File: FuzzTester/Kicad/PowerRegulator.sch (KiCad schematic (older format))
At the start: 10 parts, among them J5 TestPower_PinHeader, J6 9V Power JST XH, U1 AMS1117-5.0, U2 AMS1117-3.3

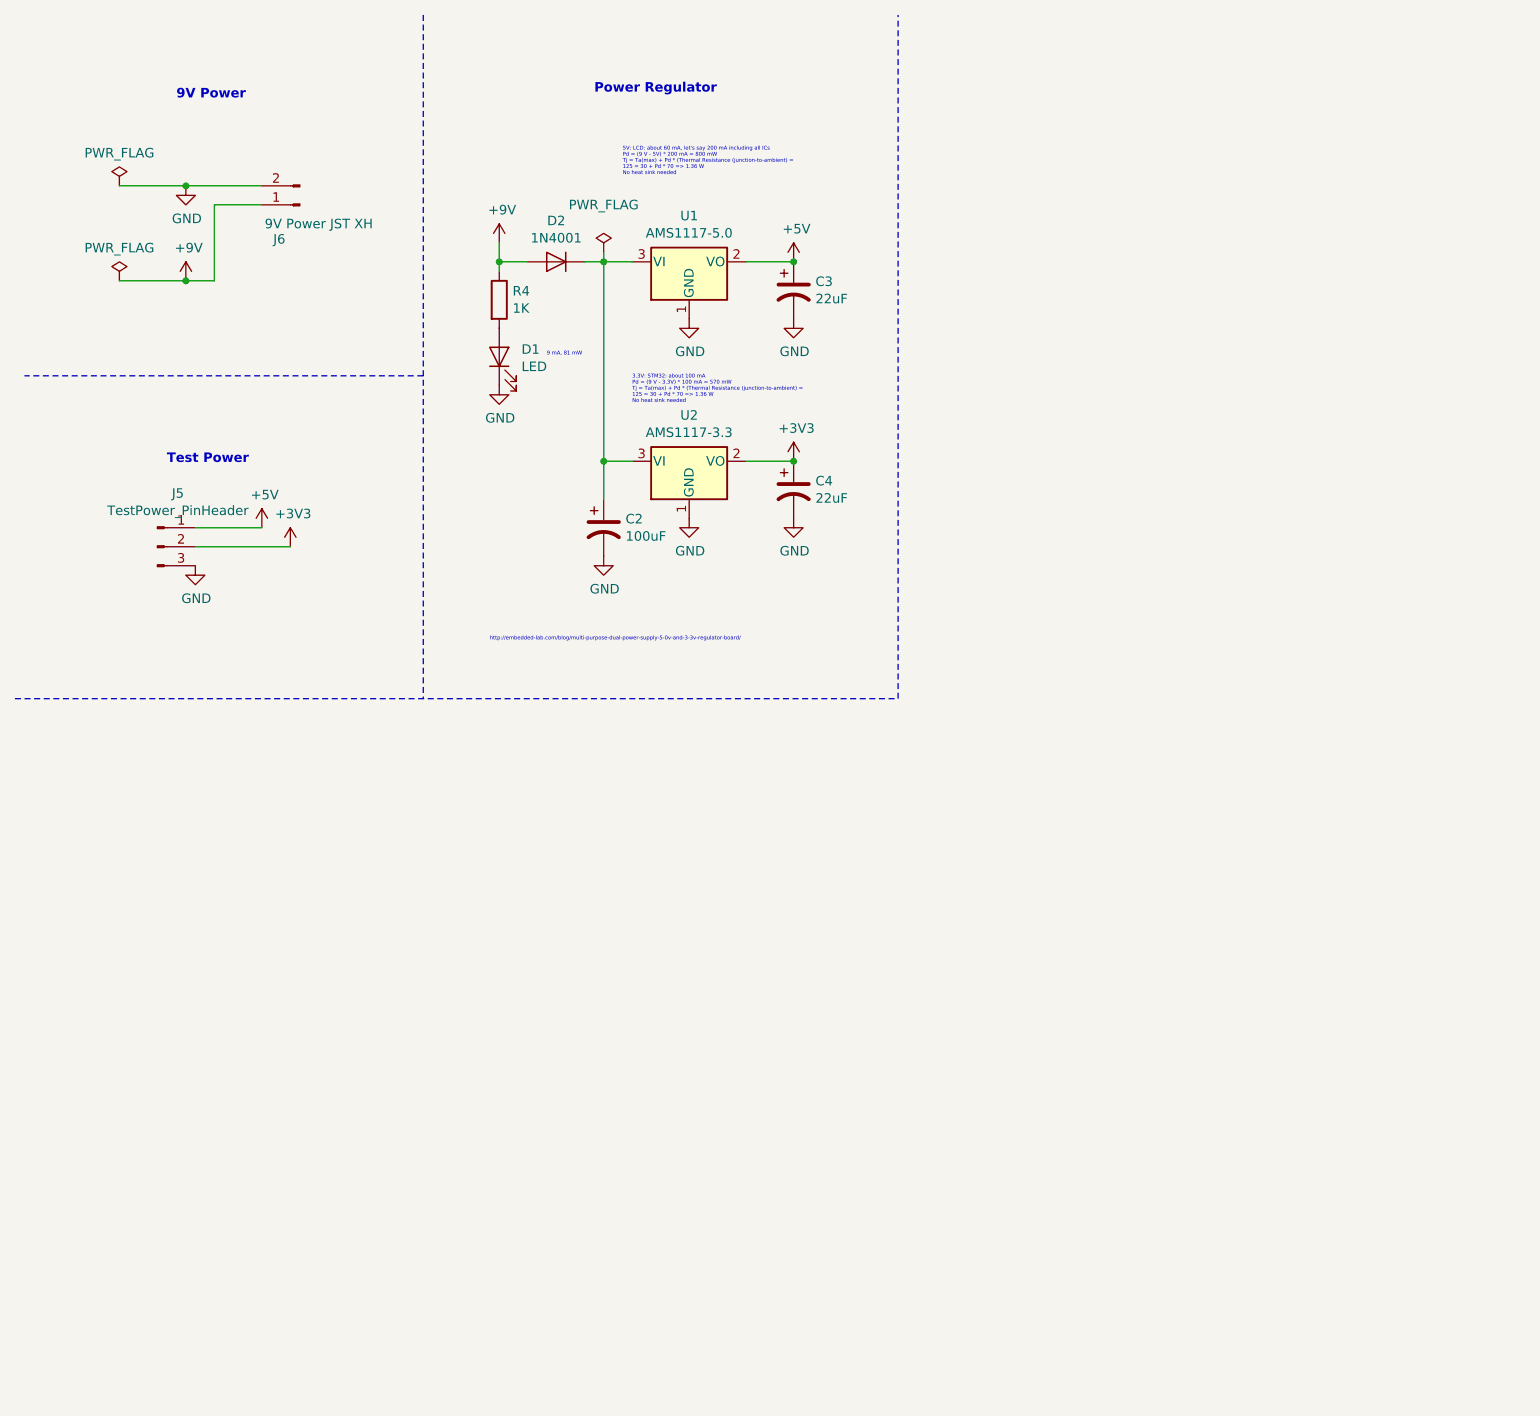
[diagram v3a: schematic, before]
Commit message: Power regulator -9V
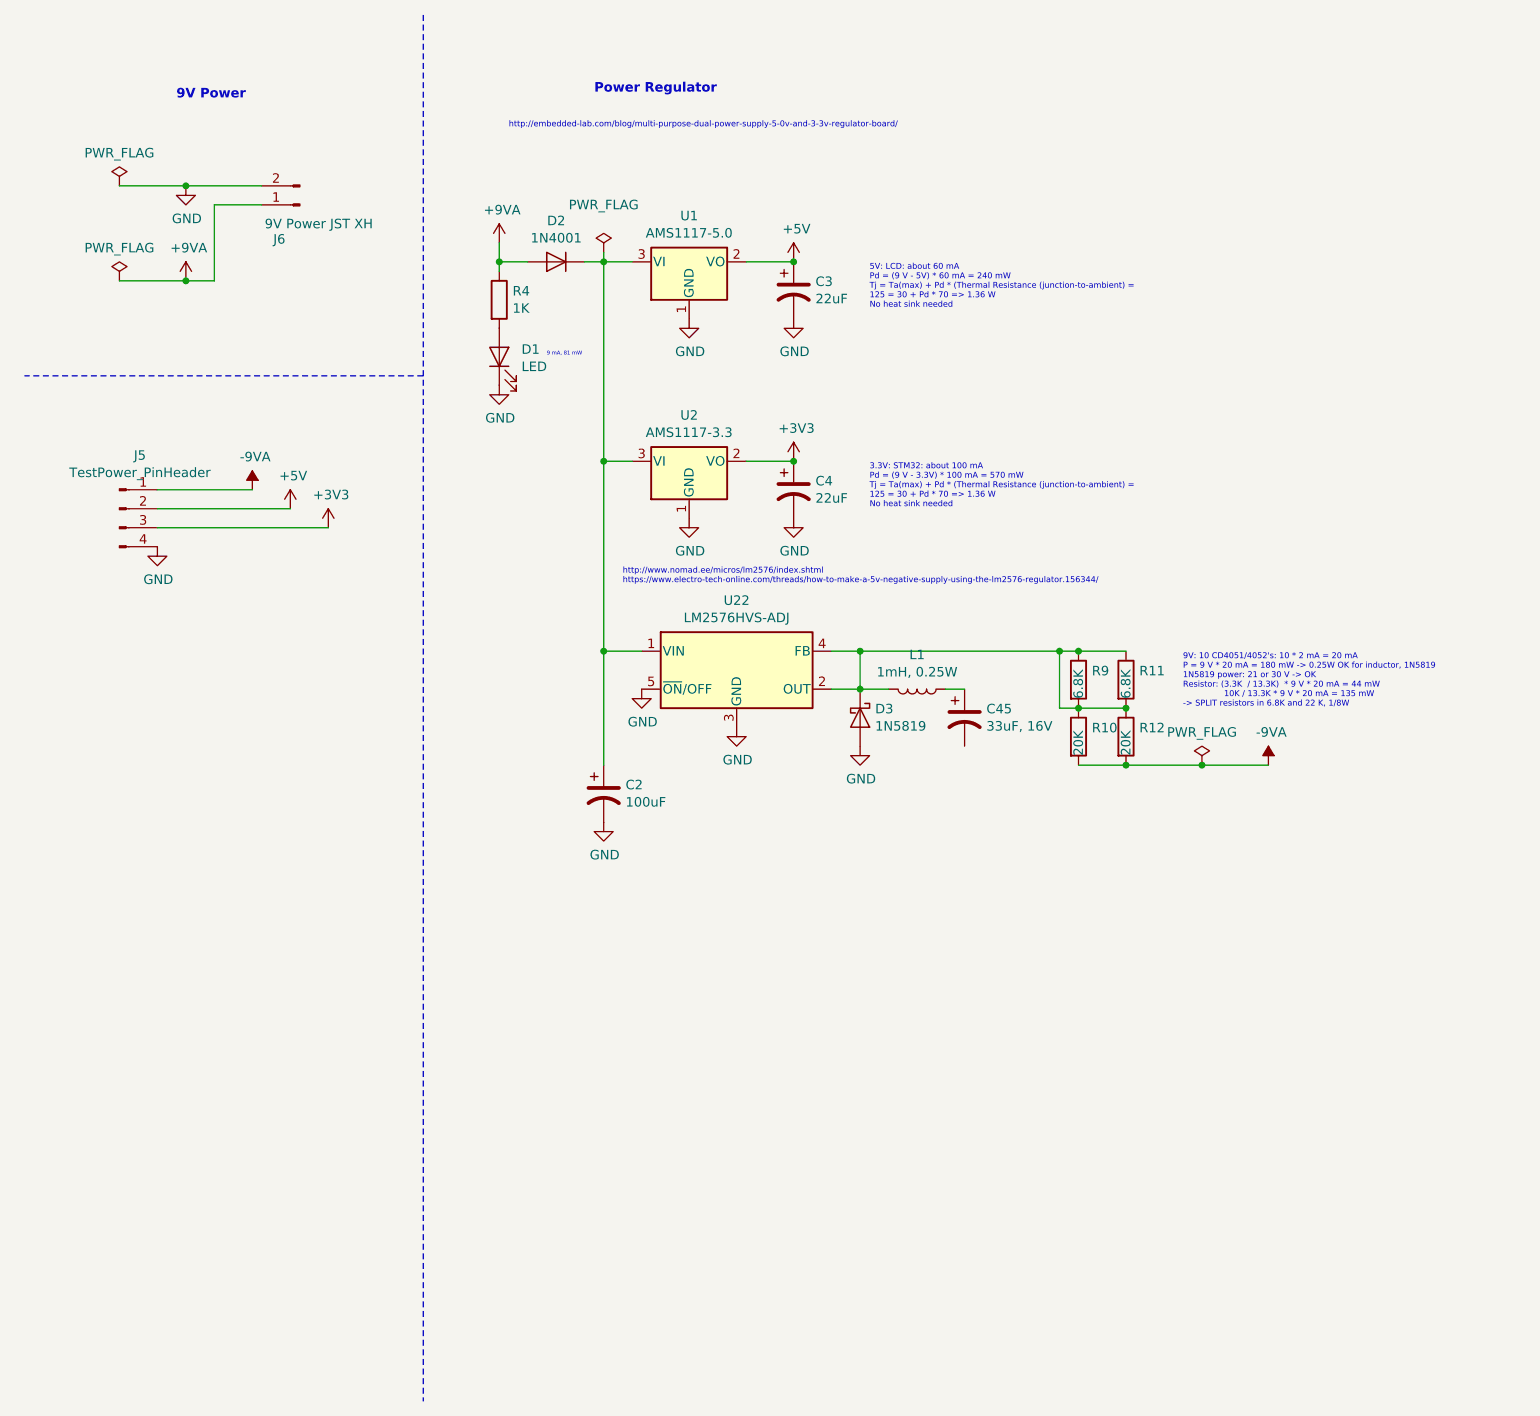
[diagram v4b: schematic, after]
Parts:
- removed J5: TestPower_PinHeader, Connector_PinHeader_2.54mm:PinHeader_1x03_P2.54mm_Vertical, symbol Connector:Conn_01x03_Male
- added C45: 33uF, 16V, symbol Device:CP1
- added D3: 1N5819, Diode_THT:D_DO-41_SOD81_P10.16mm_Horizontal, symbol Diode:1N5819
- added J5: TestPower_PinHeader, symbol Connector:Conn_01x04_Male
- added L1: 1mH, 0.25W, symbol Device:L
- added R10, R12: 20K, symbol Device:R
- added R11, R9: 6.8K, symbol Device:R
- added U22: LM2576HVS-ADJ, Package_TO_SOT_SMD:TO-263-5_TabPin3, symbol Regulator_Switching:LM2576HVS-ADJ
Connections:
- net +3V3: now also J5.3 (Pin_3)
- net +5V: now also J5.2 (Pin_2)
- net GND: now also D3.2 (A), J5.4 (Pin_4), U22.3 (GND), U22.5 (~ON~/OFF)
- net at C2.1, D2.1 (K), U1.3 (VI)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: now also U22.1 (VIN)
- net +9V renamed +9VA
- new net: D3.1 (K), L1.2, R10.1, R11.1, R11.2, R12.1, R9.1, R9.2, U22.2 (OUT), U22.4 (FB)
- new net: C45.1, L1.1
- new net -9VA: J5.1 (Pin_1), R10.2, R12.2
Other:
- note added: "5V: LCD: about 60 mA\nPd = (9 V - 5V) * 60 mA = 240 mW\nTj = Ta(max) + Pd * (Thermal Resistance (junction-to-ambient) =\n125 = 30 + Pd * 70 => 1.36 W\nNo heat sink needed"
- note added: "9V: 10 CD4051/4052's: 10 * 2 mA = 20 mA\nP = 9 V * 20 mA = 180 mW -> 0.25W OK for inductor, 1N5819\n1N5819 power: 21 or 30 V -> OK\nResistor: (3.3K / 13.3K) * 9 V * 20 mA = 44 mW\n 10K / 13.3K * 9 V * 20 mA = 135 mW\n-> SPLIT resistors in 6.8K and 22 K, 1/8W\n"
- note added: "http://www.nomad.ee/micros/lm2576/index.shtml"
- note added: "https://www.electro-tech-online.com/threads/how-to-make-a-5v-negative-supply-using-the-lm2576-regulator.156344/"
- note removed: "5V: LCD: about 60 mA, let's say 200 mA including all ICs\nPd = (9 V - 5V) * 200 mA = 800 mW\nTj = Ta(max) + Pd * (Thermal Resistance (junction-to-ambient) =\n125 = 30 + Pd * 70 => 1.36 W\nNo heat sink needed"
- note removed: "Test Power\n\n"
- moved on the sheet: C2

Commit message: PCB Placement 100x82
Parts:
- removed C45: 33uF, 16V, symbol Device:CP1
- removed D3: 1N5819, Diode_THT:D_DO-41_SOD81_P10.16mm_Horizontal, symbol Diode:1N5819
- removed L1: 1mH, 0.25W, symbol Device:L
- removed R10, R12: 20K, symbol Device:R
- removed R11, R9: 6.8K, symbol Device:R
- removed U22: LM2576HVS-ADJ, Package_TO_SOT_SMD:TO-263-5_TabPin3, symbol Regulator_Switching:LM2576HVS-ADJ
- J5: value TestPower_PinHeader -> PowerTest_PinHeader; footprint (none) -> Connector_PinHeader_2.54mm:PinHeader_1x04_P2.54mm_Vertical
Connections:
- net labels added: +9V
- net labels removed: +9VA, -9VA
- wire segments 36 -> 19
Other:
- note added: "Power Test Connector\n"
- note removed: "9V: 10 CD4051/4052's: 10 * 2 mA = 20 mA\nP = 9 V * 20 mA = 180 mW -> 0.25W OK for inductor, 1N5819\n1N5819 power: 21 or 30 V -> OK\nResistor: (3.3K / 13.3K) * 9 V * 20 mA = 44 mW\n 10K / 13.3K * 9 V * 20 mA = 135 mW\n-> SPLIT resistors in 6.8K and 22 K, 1/8W\n"
- moved on the sheet: C2

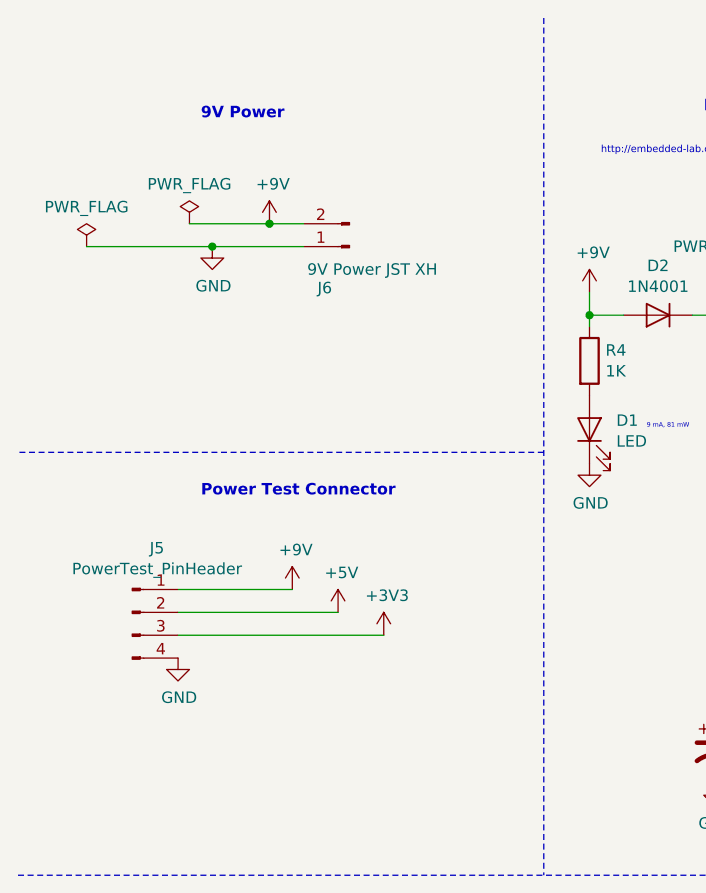
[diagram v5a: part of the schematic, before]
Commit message: GNDA, PCB DRC fixed
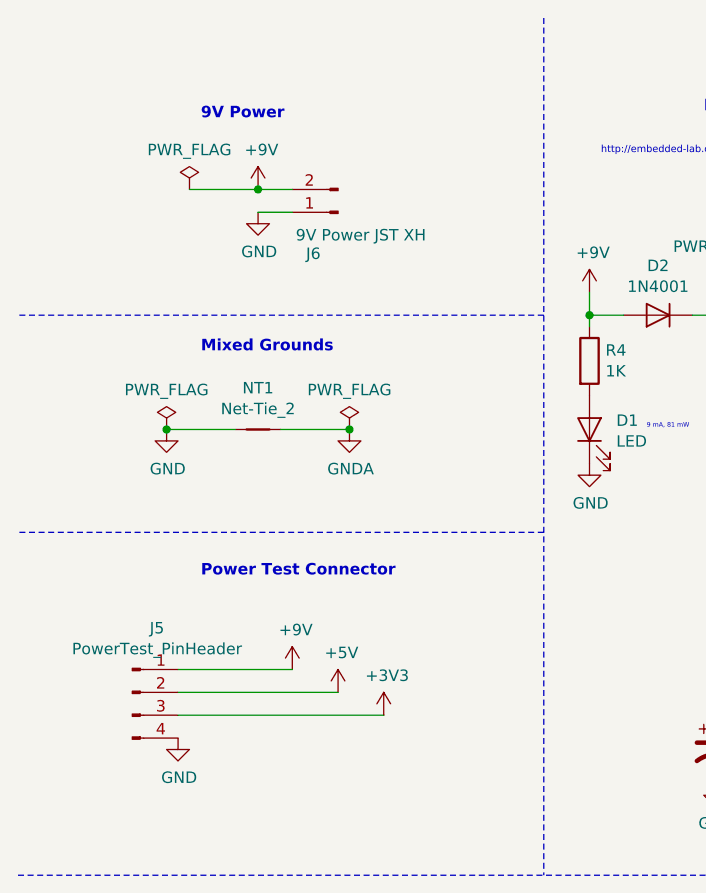
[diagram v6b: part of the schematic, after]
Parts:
- added NT1: Net-Tie_2, NetTie:NetTie-2_SMD_Pad2.0mm, symbol Device:Net-Tie_2
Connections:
- net labels added: GNDA
- wire segments 19 -> 20
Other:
- note added: "Mixed Grounds\n\n"
- moved on the sheet: J5, J6
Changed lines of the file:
@@
 L power:PWR_FLAG #FLG?
 U 1 1 5E8DF964
-P 1250 1400
+P 1250 1250
 AR Path="/5E8DF964" Ref="#FLG?"  Part="1"
 AR Path="/5E8D81C7/5E8DF964" Ref="#FLG01"  Part="1"
-F 0 "#FLG01" H 1250 1475 50  0001 C CNN
-F 1 "PWR_FLAG" H 1250 1573 50  0000 C CNN
-F 2 "" H 1250 1400 50  0001 C CNN
-F 3 "~" H 1250 1400 50  0001 C CNN
-	1    1250 1400
+F 0 "#FLG01" H 1250 1325 50  0001 C CNN
+F 1 "PWR_FLAG" H 1250 1423 50  0000 C CNN
+F 2 "" H 1250 1250 50  0001 C CNN
+F 3 "~" H 1250 1250 50  0001 C CNN
+	1    1250 1250
 	1    0    0    -1
 $EndComp
@@
 L power:GND #PWR?
 U 1 1 5E8DF96C
-P 1350 1500
+P 1550 1350
 AR Path="/5E8DF96C" Ref="#PWR?"  Part="1"
 AR Path="/5E8D81C7/5E8DF96C" Ref="#PWR07"  Part="1"
-F 0 "#PWR07" H 1350 1250 50  0001 C CNN
-F 1 "GND" H 1355 1327 50  0000 C CNN
-F 2 "" H 1350 1500 50  0001 C CNN
-F 3 "" H 1350 1500 50  0001 C CNN
-	1    1350 1500
+F 0 "#PWR07" H 1550 1100 50  0001 C CNN
+F 1 "GND" H 1555 1177 50  0000 C CNN
+F 2 "" H 1550 1350 50  0001 C CNN
+F 3 "" H 1550 1350 50  0001 C CNN
+	1    1550 1350
 	1    0    0    -1
 $EndComp
@@
 L Connector:Conn_01x02_Male J?
 U 1 1 5E8DF958
-P 1950 1500
+P 1900 1350
 AR Path="/5E8DF958" Ref="J?"  Part="1"
 AR Path="/5E8D81C7/5E8DF958" Ref="J6"  Part="1"
-F 0 "J6" H 2058 1681 50  0000 C CNN
-F 1 "9V Power JST XH" H 1850 1600 50  0000 C CNN
-F 2 "Connector_JST:JST_XH_B2B-XH-A_1x02_P2.50mm_Vertical" H 1950 1500 50  0001 C CNN
-F 3 "~" H 1950 1500 50  0001 C CNN
-	1    1950 1500
+F 0 "J6" H 2008 1531 50  0000 C CNN
+F 1 "9V Power JST XH" H 1800 1450 50  0000 C CNN
+F 2 "Connector_JST:JST_XH_B2B-XH-A_1x02_P2.50mm_Vertical" H 1900 1350 50  0001 C CNN
+F 3 "~" H 1900 1350 50  0001 C CNN
+	1    1900 1350
 	-1   0    0    1
 $EndComp
@@
 L power:+5V #PWR0103
 U 1 1 5FACFDD8
-P 1900 3100
-F 0 "#PWR0103" H 1900 2950 50  0001 C CNN
-F 1 "+5V" H 1915 3273 50  0000 C CNN
-F 2 "" H 1900 3100 50  0001 C CNN
-F 3 "" H 1900 3100 50  0001 C CNN
-	1    1900 3100
+P 1900 3450
+F 0 "#PWR0103" H 1900 3300 50  0001 C CNN
+F 1 "+5V" H 1915 3623 50  0000 C CNN
+F 2 "" H 1900 3450 50  0001 C CNN
+F 3 "" H 1900 3450 50  0001 C CNN
+	1    1900 3450
 	1    0    0    -1
 $EndComp
@@
 L power:+3V3 #PWR0104
 U 1 1 5FAD14EB
-P 2100 3200
-F 0 "#PWR0104" H 2100 3050 50  0001 C CNN
-F 1 "+3V3" H 2115 3373 50  0000 C CNN
-F 2 "" H 2100 3200 50  0001 C CNN
-F 3 "" H 2100 3200 50  0001 C CNN
-	1    2100 3200
+P 2100 3550
+F 0 "#PWR0104" H 2100 3400 50  0001 C CNN
+F 1 "+3V3" H 2115 3723 50  0000 C CNN
+F 2 "" H 2100 3550 50  0001 C CNN
+F 3 "" H 2100 3550 50  0001 C CNN
+	1    2100 3550
 	1    0    0    -1
 $EndComp
@@
 L power:GND #PWR?
 U 1 1 5FAD2482
-P 1200 3300
+P 1200 3650
 AR Path="/5FAD2482" Ref="#PWR?"  Part="1"
 AR Path="/5E8D81C7/5FAD2482" Ref="#PWR0105"  Part="1"
-F 0 "#PWR0105" H 1200 3050 50  0001 C CNN
-F 1 "GND" H 1205 3127 50  0000 C CNN
-F 2 "" H 1200 3300 50  0001 C CNN
-F 3 "" H 1200 3300 50  0001 C CNN
-	1    1200 3300
+F 0 "#PWR0105" H 1200 3400 50  0001 C CNN
+F 1 "GND" H 1205 3477 50  0000 C CNN
+F 2 "" H 1200 3650 50  0001 C CNN
+F 3 "" H 1200 3650 50  0001 C CNN
+	1    1200 3650
 	1    0    0    -1
 $EndComp
@@
 L power:PWR_FLAG #FLG?
 U 1 1 5FBDD6C7
-P 800 1500
+P 1150 2300
 AR Path="/5FBDD6C7" Ref="#FLG?"  Part="1"
 AR Path="/5E8D81C7/5FBDD6C7" Ref="#FLG0105"  Part="1"
-F 0 "#FLG0105" H 800 1575 50  0001 C CNN
-F 1 "PWR_FLAG" H 800 1673 50  0000 C CNN
-F 2 "" H 800 1500 50  0001 C CNN
-F 3 "~" H 800 1500 50  0001 C CNN
-	1    800  1500
-	1    0    0    -1
-$EndComp
-Wire Wire Line
-	800  1500 1350 1500
+F 0 "#FLG0105" H 1150 2375 50  0001 C CNN
+F 1 "PWR_FLAG" H 1150 2473 50  0000 C CNN
+F 2 "" H 1150 2300 50  0001 C CNN
+F 3 "~" H 1150 2300 50  0001 C CNN
+	1    1150 2300
+	1    0    0    -1
+$EndComp
 $Comp
 L Device:CP1 C4
@@
 	2800 500  2800 4250
 Wire Notes Line
-	2800 2400 500  2400
+	2800 2750 500  2750
 Text Notes 3650 3500 0    31   ~ 0
 https://www.electro-tech-online.com/threads/how-to-make-a-5v-negative-supply-using-the-lm2576-regulator.156344/
@@
 L Connector:Conn_01x04_Male J5
 U 1 1 5E90BAA0
-P 1000 3100
-F 0 "J5" H 1108 3381 50  0000 C CNN
-F 1 "PowerTest_PinHeader" H 1108 3290 50  0000 C CNN
-F 2 "Connector_PinHeader_2.54mm:PinHeader_1x04_P2.54mm_Vertical" H 1000 3100 50  0001 C CNN
-F 3 "~" H 1000 3100 50  0001 C CNN
-	1    1000 3100
-	1    0    0    -1
-$EndComp
-Wire Wire Line
-	1200 3200 2100 3200
-Wire Wire Line
-	1900 3100 1200 3100
-Wire Wire Line
-	1200 3000 1700 3000
+P 1000 3450
+F 0 "J5" H 1108 3731 50  0000 C CNN
+F 1 "PowerTest_PinHeader" H 1108 3640 50  0000 C CNN
+F 2 "Connector_PinHeader_2.54mm:PinHeader_1x04_P2.54mm_Vertical" H 1000 3450 50  0001 C CNN
+F 3 "~" H 1000 3450 50  0001 C CNN
+	1    1000 3450
+	1    0    0    -1
+$EndComp
+Wire Wire Line
+	1200 3550 2100 3550
+Wire Wire Line
+	1900 3450 1200 3450
+Wire Wire Line
+	1200 3350 1700 3350
 $Comp
 L power:+9V #PWR0112
 U 1 1 5EAD02BC
-P 1700 3000
-F 0 "#PWR0112" H 1700 2850 50  0001 C CNN
-F 1 "+9V" H 1715 3173 50  0000 C CNN
-F 2 "" H 1700 3000 50  0001 C CNN
-F 3 "" H 1700 3000 50  0001 C CNN
-	1    1700 3000
+P 1700 3350
+F 0 "#PWR0112" H 1700 3200 50  0001 C CNN
+F 1 "+9V" H 1715 3523 50  0000 C CNN
+F 2 "" H 1700 3350 50  0001 C CNN
+F 3 "" H 1700 3350 50  0001 C CNN
+	1    1700 3350
 	1    0    0    -1
 $EndComp
@@
 $EndComp
 Wire Wire Line
-	1250 1400 1600 1400
+	1250 1250 1550 1250
 $Comp
 L power:+9V #PWR0115
 U 1 1 5EAD27B5
-P 1600 1400
-F 0 "#PWR0115" H 1600 1250 50  0001 C CNN
-F 1 "+9V" H 1615 1573 50  0000 C CNN
-F 2 "" H 1600 1400 50  0001 C CNN
-F 3 "" H 1600 1400 50  0001 C CNN
-	1    1600 1400
-	1    0    0    -1
-$EndComp
-Connection ~ 1600 1400
-Wire Wire Line
-	1600 1400 1750 1400
+P 1550 1250
+F 0 "#PWR0115" H 1550 1100 50  0001 C CNN
+F 1 "+9V" H 1565 1423 50  0000 C CNN
+F 2 "" H 1550 1250 50  0001 C CNN
+F 3 "" H 1550 1250 50  0001 C CNN
+	1    1550 1250
+	1    0    0    -1
+$EndComp
+Connection ~ 1550 1250
+Wire Wire Line
+	1550 1250 1700 1250
 Wire Wire Line
 	3550 2850 3550 3550
@@
 Wire Wire Line
 	3550 1800 3550 2850
-Text Notes 1300 2600 0    50   ~ 10
+Text Notes 1300 2950 0    50   ~ 10
 Power Test Connector\n
 Wire Wire Line
-	1350 1500 1750 1500
-Connection ~ 1350 1500
+	1550 1350 1700 1350
+Text Notes 1300 2050 0    50   ~ 10
+Mixed Grounds\n\n
+Wire Notes Line
+	2800 1800 500  1800
+$Comp
+L power:GND #PWR?
+U 1 1 5EA16D11
+P 1150 2300
+AR Path="/5EA16D11" Ref="#PWR?"  Part="1"
+AR Path="/5E8D81C7/5EA16D11" Ref="#PWR059"  Part="1"
+F 0 "#PWR059" H 1150 2050 50  0001 C CNN
+F 1 "GND" H 1155 2127 50  0000 C CNN
+F 2 "" H 1150 2300 50  0001 C CNN
+F 3 "" H 1150 2300 50  0001 C CNN
+	1    1150 2300
+	1    0    0    -1
+$EndComp
+$Comp
+L power:GNDA #PWR063
+U 1 1 5EA16F95
+P 1950 2300
+F 0 "#PWR063" H 1950 2050 50  0001 C CNN
+F 1 "GNDA" H 1955 2127 50  0000 C CNN
+F 2 "" H 1950 2300 50  0001 C CNN
+F 3 "" H 1950 2300 50  0001 C CNN
+	1    1950 2300
+	1    0    0    -1
+$EndComp
+$Comp
+L Device:Net-Tie_2 NT1
+U 1 1 5EA1781D
+P 1550 2300
+F 0 "NT1" H 1550 2481 50  0000 C CNN
+F 1 "Net-Tie_2" H 1550 2390 50  0000 C CNN
+F 2 "NetTie:NetTie-2_SMD_Pad2.0mm" H 1550 2300 50  0001 C CNN
+F 3 "~" H 1550 2300 50  0001 C CNN
+	1    1550 2300
+	1    0    0    -1
+$EndComp
+Wire Wire Line
+	1650 2300 1950 2300
+$Comp
+L power:PWR_FLAG #FLG?
+U 1 1 5EA23D2A
+P 1950 2300
+AR Path="/5EA23D2A" Ref="#FLG?"  Part="1"
+AR Path="/5E8D81C7/5EA23D2A" Ref="#FLG0102"  Part="1"
+F 0 "#FLG0102" H 1950 2375 50  0001 C CNN
+F 1 "PWR_FLAG" H 1950 2473 50  0000 C CNN
+F 2 "" H 1950 2300 50  0001 C CNN
+F 3 "~" H 1950 2300 50  0001 C CNN
+	1    1950 2300
+	1    0    0    -1
+$EndComp
+Connection ~ 1950 2300
+Wire Wire Line
+	1150 2300 1450 2300
+Connection ~ 1150 2300
 $EndSCHEMATC
